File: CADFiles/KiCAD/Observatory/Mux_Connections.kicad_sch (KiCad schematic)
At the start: 3 parts, among them U2 Scope 1 Mux, U3 Wave Gen. Mux, U4 Scope 2 Mux

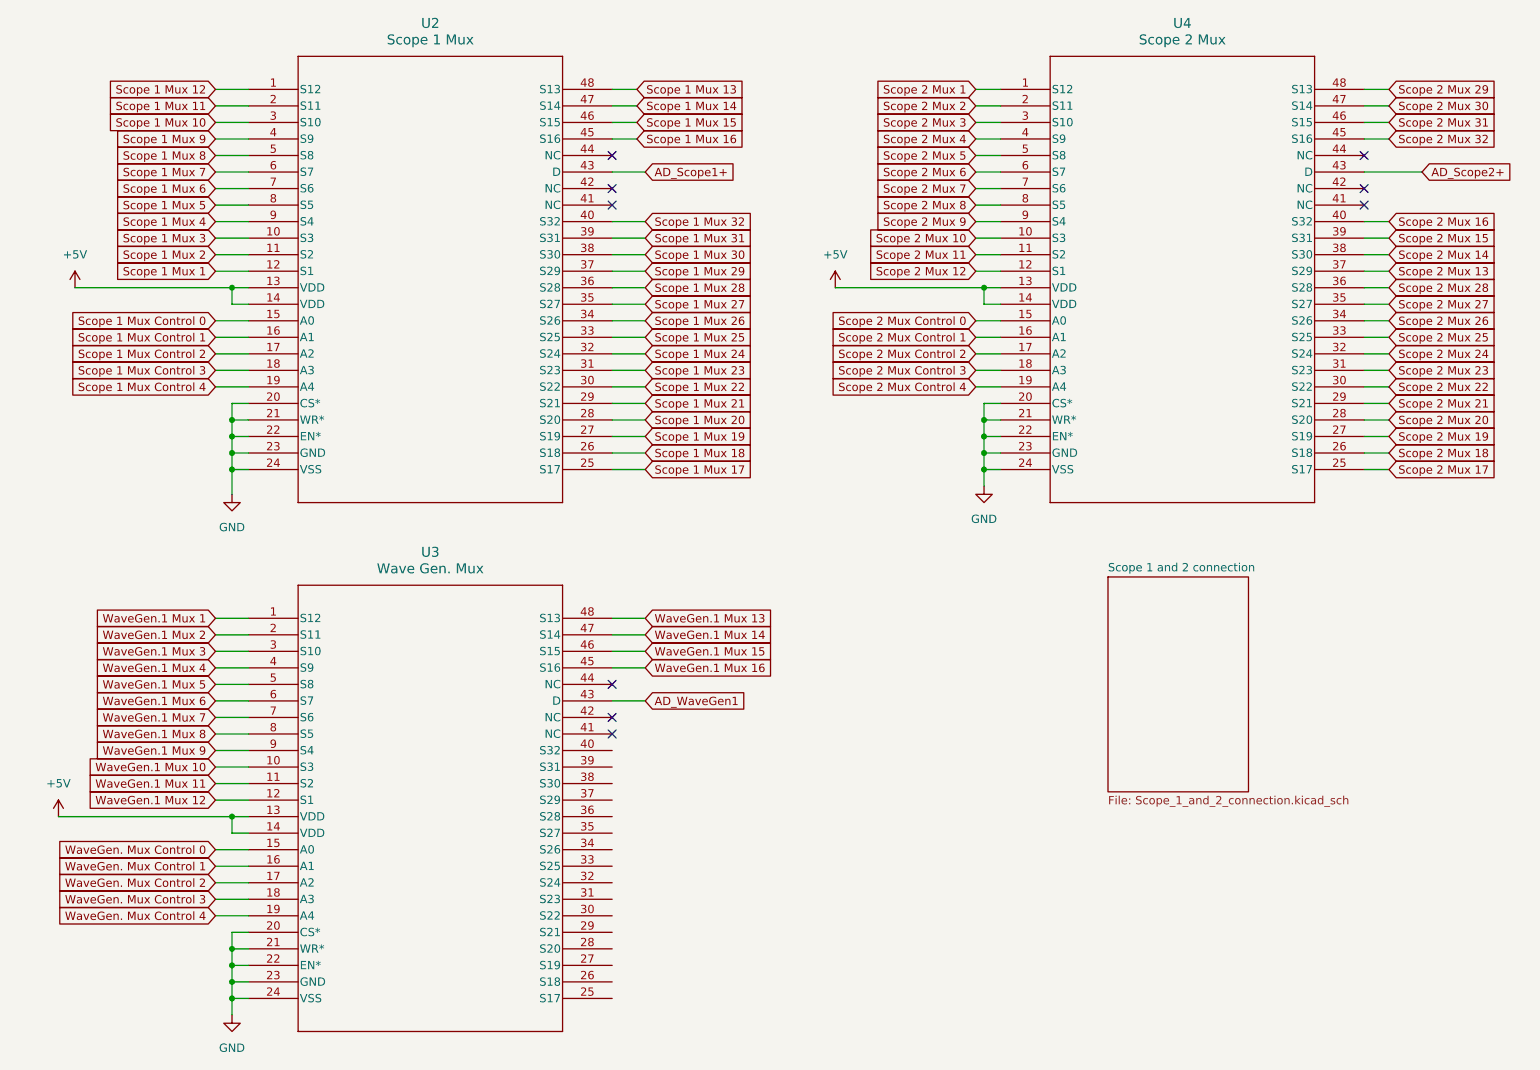
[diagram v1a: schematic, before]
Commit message: All nets routed.
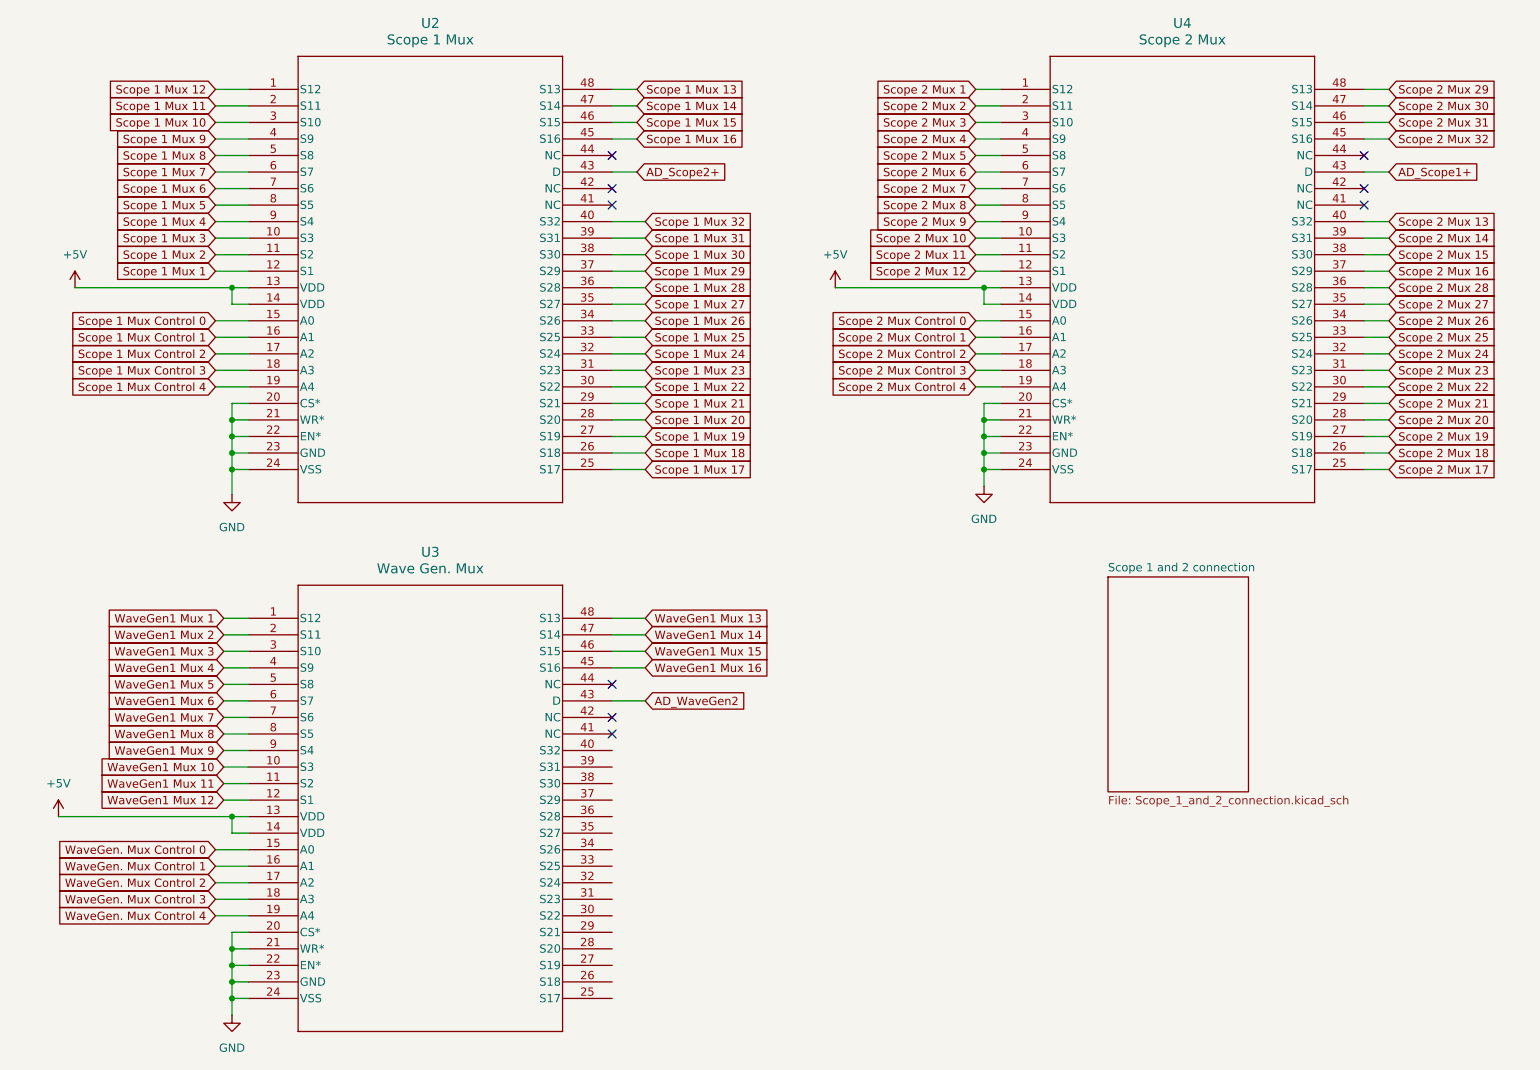
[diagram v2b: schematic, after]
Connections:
- net AD_Scope1+: now also U4.43 (D); no longer U2.43 (D)
- net AD_Scope2+: now also U2.43 (D); no longer U4.43 (D)
- net Scope 2 Mux  13: now also U4.40 (S32); no longer U4.37 (S29)
- net Scope 2 Mux  14: now also U4.39 (S31); no longer U4.38 (S30)
- net Scope 2 Mux  15: now also U4.38 (S30); no longer U4.39 (S31)
- net Scope 2 Mux  16: now also U4.37 (S29); no longer U4.40 (S32)
- net AD_WaveGen1 renamed AD_WaveGen2
- net WaveGen.1 Mux  1 renamed WaveGen1 Mux  1
- net WaveGen.1 Mux  10 renamed WaveGen1 Mux  10
- net WaveGen.1 Mux  11 renamed WaveGen1 Mux  11
- net WaveGen.1 Mux  12 renamed WaveGen1 Mux  12
- net WaveGen.1 Mux  13 renamed WaveGen1 Mux  13
- net WaveGen.1 Mux  14 renamed WaveGen1 Mux  14
- net WaveGen.1 Mux  15 renamed WaveGen1 Mux  15
- net WaveGen.1 Mux  16 renamed WaveGen1 Mux  16
- net WaveGen.1 Mux  2 renamed WaveGen1 Mux  2
- net WaveGen.1 Mux  3 renamed WaveGen1 Mux  3
- net WaveGen.1 Mux  4 renamed WaveGen1 Mux  4
- net WaveGen.1 Mux  5 renamed WaveGen1 Mux  5
- net WaveGen.1 Mux  6 renamed WaveGen1 Mux  6
- net WaveGen.1 Mux  7 renamed WaveGen1 Mux  7
- net WaveGen.1 Mux  8 renamed WaveGen1 Mux  8
- net WaveGen.1 Mux  9 renamed WaveGen1 Mux  9

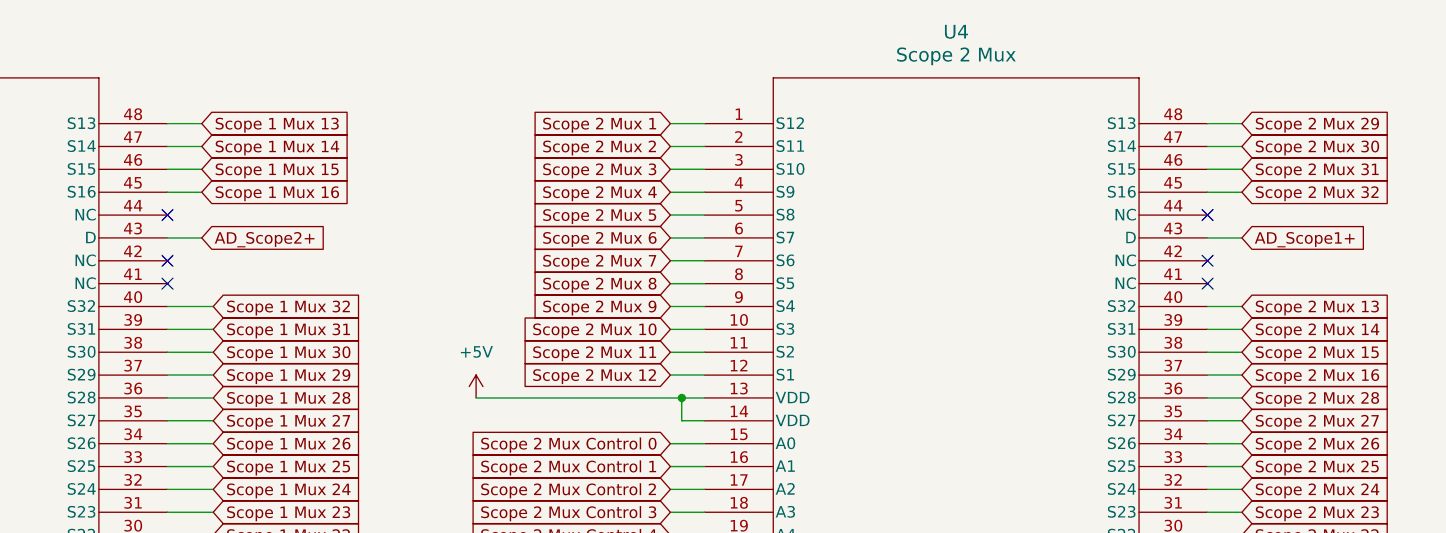
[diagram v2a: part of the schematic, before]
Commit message: DRC pass. Labels Added.
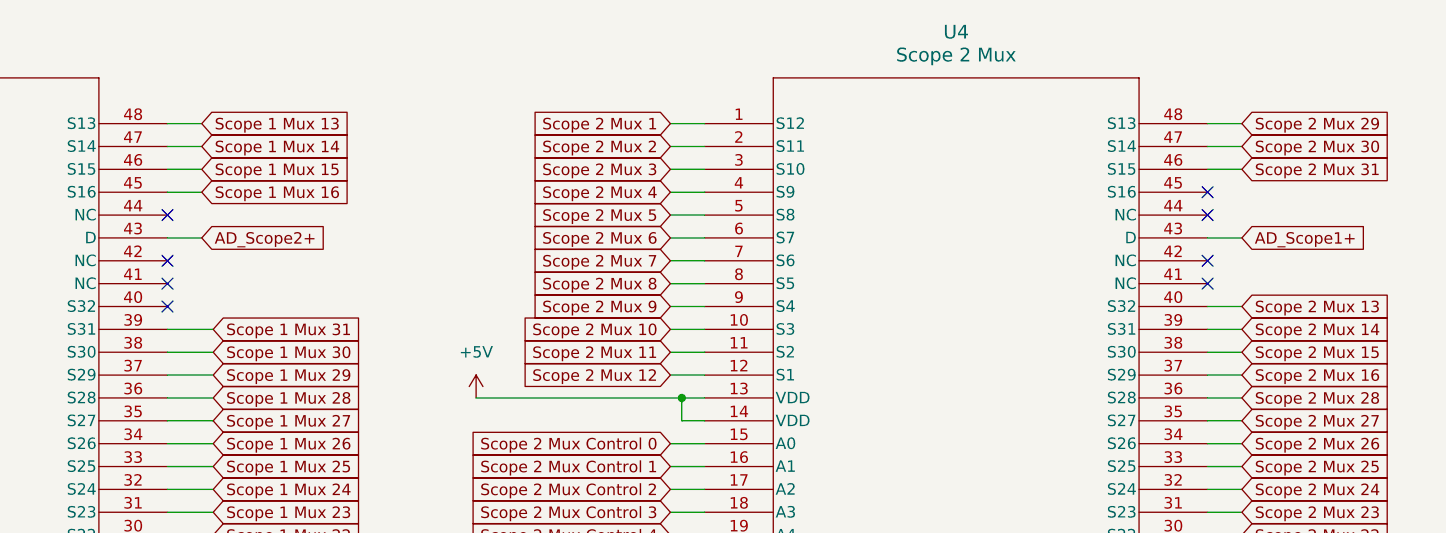
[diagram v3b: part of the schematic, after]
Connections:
- net Scope 1 Mux  32: no longer names the net of U2.40 (S32)
- net Scope 2 Mux  32: no longer names the net of U4.45 (S16)
- no-connect marks 9 -> 11
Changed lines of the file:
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@@
 	)
 	(no_connect
+		(at 217.17 39.37)
+	)
+	(no_connect
+		(at 101.6 52.07)
+	)
+	(no_connect
 		(at 101.6 123.19)
 	)
@@
 	(wire
 		(pts
-			(xy 217.17 39.37) (xy 220.98 39.37)
-		)
-		(stroke
-			(width 0)
-			(type default)
-		)
-	)
-	(wire
-		(pts
 			(xy 43.18 143.51) (xy 45.72 143.51)
 		)
@@
 	(wire
 		(pts
-			(xy 101.6 52.07) (xy 106.68 52.07)
-		)
-		(stroke
-			(width 0)
-			(type default)
-		)
-	)
-	(wire
-		(pts
 			(xy 40.64 31.75) (xy 45.72 31.75)
 		)
@@
 		)
 	)
-	(global_label "Scope 2 Mux  32"
-		(shape input)
-		(at 220.98 39.37 0)
-		(fields_autoplaced yes)
-		(effects
-			(font
-				(size 1.27 1.27)
-			)
-			(justify left)
-		)
-		(property "Intersheetrefs" "${INTERSHEET_REFS}"
-			(at 240.7773 39.37 0)
-			(effects
-				(font
-					(size 1.27 1.27)
-				)
-				(justify left)
-				(hide yes)
-			)
-		)
-	)
 	(global_label "WaveGen1 Mux  11"
 		(shape input)
@@
 				(hide yes)
 			)
-		)
-	)
-	(global_label "Scope 1 Mux  32"
-		(shape input)
-		(at 106.68 52.07 0)
-		(fields_autoplaced yes)
-		(effects
-			(font
-				(size 1.27 1.27)
-			)
-			(justify left)
-		)
-		(property "Intersheetrefs" "${INTERSHEET_REFS}"
-			(at 126.4773 52.07 0)
-			(effects
-				(font
-					(size 1.27 1.27)
-				)
-				(justify left)
-				(hide yes)
-			)

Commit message: AD DC(-) error fixed. Jumpers added for feet grounds and DC supplies
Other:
- company: (none) -> West Lab
- title: (none) -> SCuM Observatory
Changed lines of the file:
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@@
 	(generator_version "9.0")
 	(paper "A4")
+	(title_block
+		(title "SCuM Observatory")
+		(date "2025-03-21")
+		(rev "2")
+		(company "West Lab")
+	)
 	(junction
 		(at 43.18 90.17)
